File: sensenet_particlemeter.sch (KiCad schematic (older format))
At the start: 92 parts, among them J1 CONN_01X01, J10 CONN_01X01, J11 CONN_01X01, J12 CONN_01X01, J13 BARREL_JACK, J14 CONN_01X01, J15 CONN_01X01, J16 CONN_01X01, J17 CONN_01X01, J18 CONN_01X01, J19 CONN_01X01, J2 CONN_01X01, J20 CONN_01X01, J3 CONN_01X01, J4 CONN_01X01, J5 CONN_01X01, J6 CONN_01X01, J7 CONN_01X06, J8 CONN_01X01, J9 CONN_01X01, P1 SMA_mini, P2 SMA_mini, Q1 Q_NPN_BCV71, SW1 SW_Push, U1 wireless_patice, U10 bme280_barebone, U11 SR4G008, U2 stm32f072, U3 QUECTEL_BC95, U4 SIM, U6 M24C04, U7 M10578-A2, U8 LD39050, U9 NCP59150, Y1 8MHz

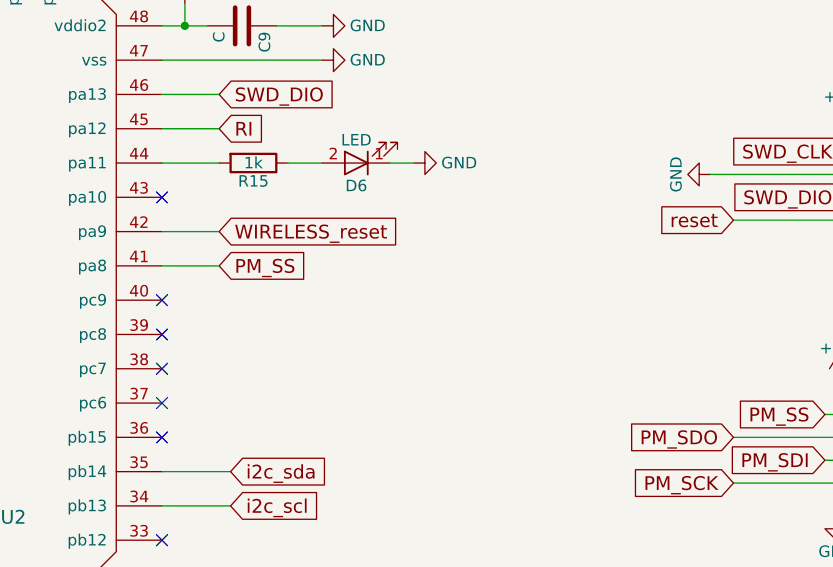
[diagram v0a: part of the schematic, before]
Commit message: added reset pin wire for quectel, fixed holes position
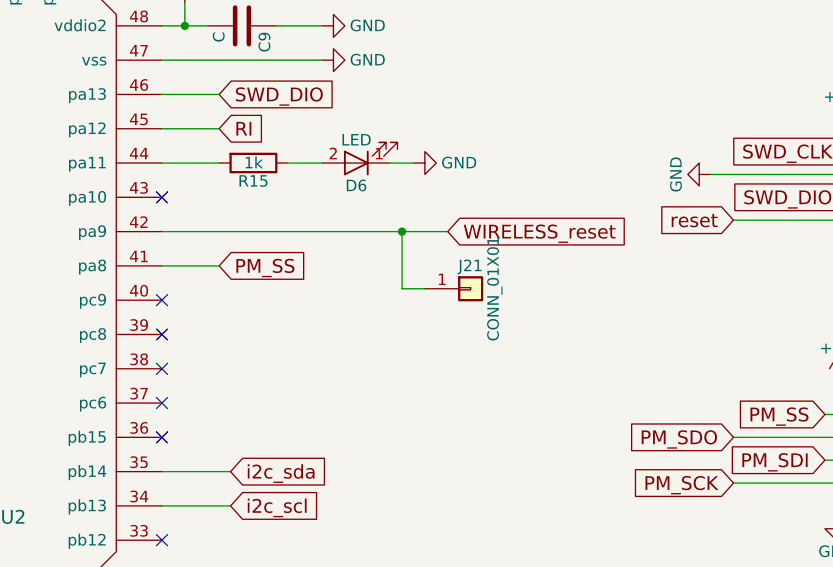
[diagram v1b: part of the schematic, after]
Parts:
- added J21: CONN_01X01, SNPM:Pin_Header_Straight_1x01_Pitch1.00mm, symbol Conn_01x01
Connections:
- net WIRELESS_reset: now also J21.1 (Pin_1)
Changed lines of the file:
@@
 Text GLabel 11550 5300 3    60   Input ~ 0
 i2c_scl
-Text GLabel 5550 2700 2    60   Input ~ 0
+Text GLabel 6550 2700 2    60   Input ~ 0
 WIRELESS_reset
 $Comp
@@
 	1950 1800 2050 1800
 Wire Wire Line
-	5300 2700 5550 2700
+	5300 2700 6550 2700
 Wire Wire Line
 	11350 7050 11600 7050
@@
 NoConn ~ 8050 10600
 NoConn ~ 8000 10200
+$Comp
+L Conn_01x01 J21
+U 1 1 5A15C8F9
+P 6650 2950
+F 0 "J21" H 6650 3050 50  0000 C CNN
+F 1 "CONN_01X01" V 6750 2950 50  0000 C CNN
+F 2 "SNPM:Pin_Header_Straight_1x01_Pitch1.00mm" H 6650 2950 50  0001 C CNN
+F 3 "" H 6650 2950 50  0001 C CNN
+	1    6650 2950
+	1    0    0    -1
+$EndComp
+Wire Wire Line
+	6350 2700 6350 2950
+Wire Wire Line
+	6350 2950 6450 2950
+Connection ~ 6350 2700
 $EndSCHEMATC

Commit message: lorawan module PCB added
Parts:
- removed C15: 1u, SNPM:SMD_0805, symbol C
- removed C16: 470u, SNPM:CP_Elec_8x10, symbol CP
- C16: renamed from C26; footprint SNPM:SMD_0805 -> SNPM:CP_Elec_8x10
- C19: value 220u -> 470u
- C23, C25: value 1u -> 10u
